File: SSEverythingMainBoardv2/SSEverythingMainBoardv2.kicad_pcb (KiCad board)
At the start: 4 copper layers, 99.1 x 81.3 mm, 71 parts, among them J1 CONN_06SILK_FEMALE_PTH, J2 CONN_06SILK_FEMALE_PTH, J4 Switch, J5 Conn_01x02, J6 Conn_01x05, J8 Conn_01x03, M1 Left MOTOR, M2 Right MOTOR, Q1 PBSS4160DS, Q2 PBSS4160DS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

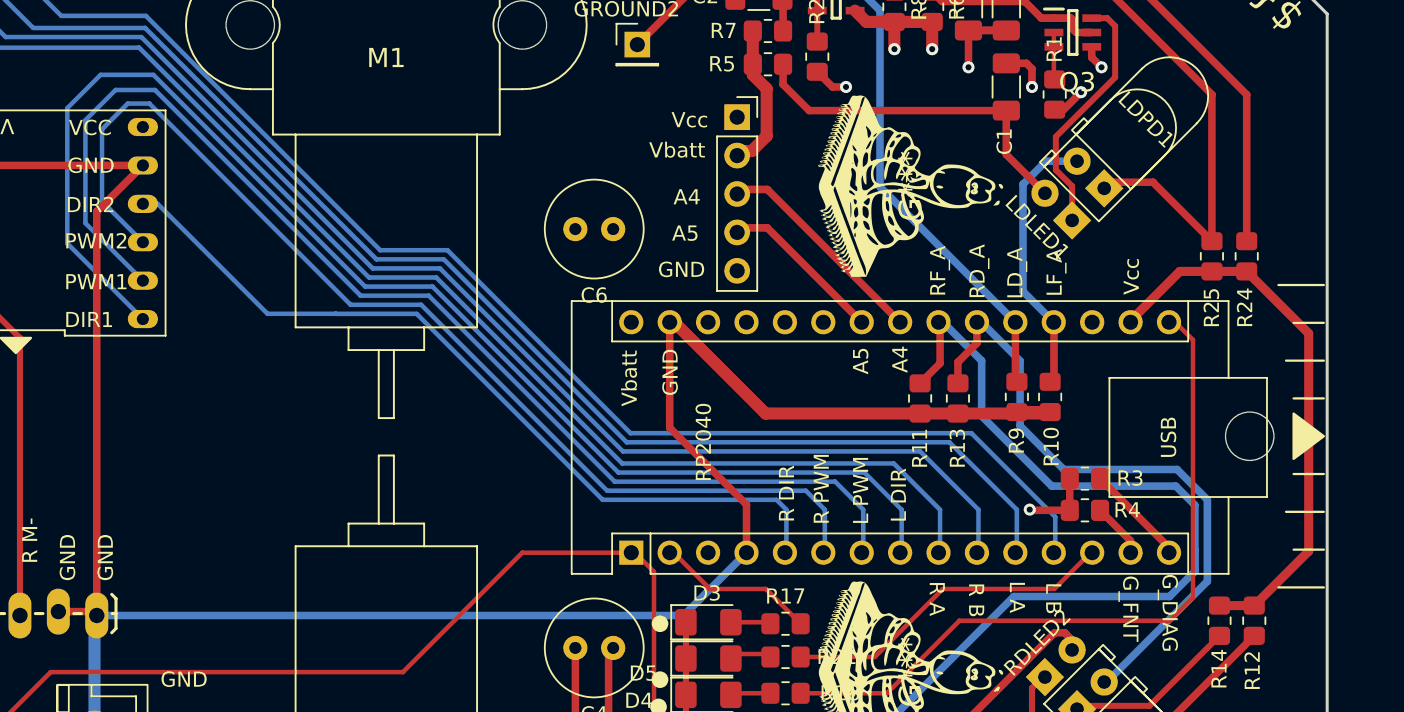
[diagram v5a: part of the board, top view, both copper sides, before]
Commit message: trace tweaks
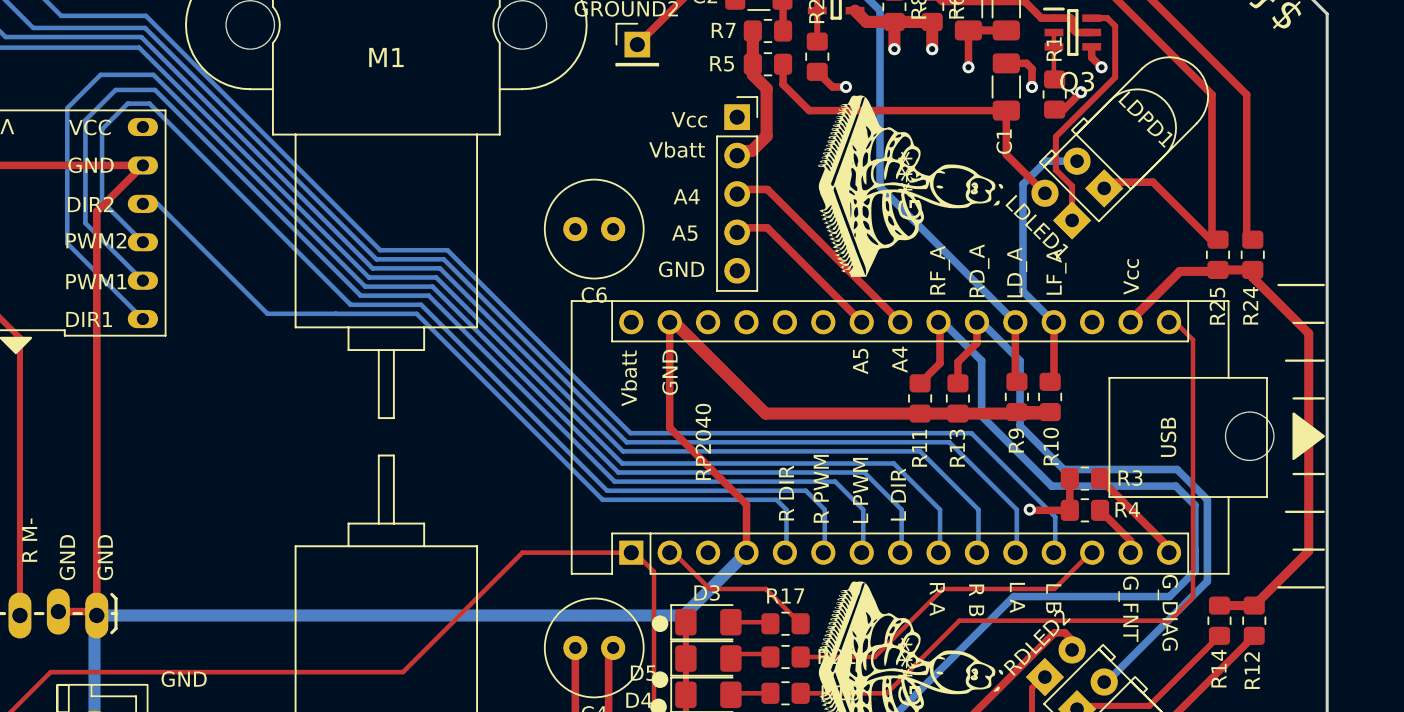
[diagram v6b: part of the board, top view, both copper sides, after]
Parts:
- moved R24 0.41 mm to (162.3, 93.0)
- moved R25 0.41 mm to (160.0, 93.0)
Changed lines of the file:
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@@
 	(footprint "Resistor_SMD:R_0805_2012Metric_Pad1.20x1.40mm_HandSolder"
 		(layer "F.Cu")
-		(at 161.9 93.1 -90)
+		(at 162.3 93 -90)
 		(descr "Resistor SMD 0805 (2012 Metric), square (rectangular) end terminal, IPC-7351 nominal with elongated pad for handsoldering. (Body size source: IPC-SM-782 page 72, https://www.pcb-3d.com/wordpress/wp-content/uploads/ipc-sm-782a_amendment_1_and_2.pdf), generated with kicad-footprint-generator")
 		(tags "resistor handsolder")
@@
 		(fp_poly
 			(pts
-				(xy -1.94 -1.21) (xy 4.49 -1.21) (xy 4.49 10.18) (xy -1.94 10.179997)
+				(xy -1.94 -1.21) (xy 4.49 -1.21) (xy 4.49 10.18) (xy -1.94 10.179999)
 			)
 			(stroke
@@
 		(fp_poly
 			(pts
-				(xy -1.94 -1.21) (xy 4.49 -1.21) (xy 4.49 10.18) (xy -1.94 10.179997)
+				(xy -1.94 -1.21) (xy 4.49 -1.21) (xy 4.49 10.18) (xy -1.94 10.179999)
 			)
 			(stroke
@@
 		(fp_poly
 			(pts
-				(xy -1.94 -1.21) (xy 4.490002 -1.21) (xy 4.49 10.18) (xy -1.94 10.18)
+				(xy -1.94 -1.21) (xy 4.490001 -1.21) (xy 4.49 10.18) (xy -1.94 10.18)
 			)
 			(stroke
@@
 		(fp_line
 			(start -1.23 1.27)
-			(end -1.229998 7.37)
+			(end -1.229999 7.37)
 			(stroke
 				(width 0.1)
@@
 			(start 3.77 7.37)
 			(mid 1.27 9.87)
-			(end -1.229998 7.37)
+			(end -1.229999 7.37)
 			(stroke
 				(width 0.1)
@@
 	(footprint "Resistor_SMD:R_0805_2012Metric_Pad1.20x1.40mm_HandSolder"
 		(layer "F.Cu")
-		(at 159.6 93.1 -90)
+		(at 160 93 -90)
 		(descr "Resistor SMD 0805 (2012 Metric), square (rectangular) end terminal, IPC-7351 nominal with elongated pad for handsoldering. (Body size source: IPC-SM-782 page 72, https://www.pcb-3d.com/wordpress/wp-content/uploads/ipc-sm-782a_amendment_1_and_2.pdf), generated with kicad-footprint-generator")
 		(tags "resistor handsolder")
@@
 		(fp_poly
 			(pts
-				(xy -1.94 -1.21) (xy 4.490002 -1.21) (xy 4.49 10.18) (xy -1.94 10.18)
+				(xy -1.94 -1.21) (xy 4.490001 -1.21) (xy 4.49 10.18) (xy -1.94 10.18)
 			)
 			(stroke
@@
 		(fp_line
 			(start -1.23 1.27)
-			(end -1.229998 7.37)
+			(end -1.229999 7.37)
 			(stroke
 				(width 0.1)
@@
 			(start 3.77 7.37)
 			(mid 1.27 9.87)
-			(end -1.229998 7.37)
+			(end -1.229999 7.37)
 			(stroke
 				(width 0.1)
@@
 		(start 85.85 116.854)
 		(end 124.666 116.854)
-		(width 0.5)
+		(width 0.8)
 		(layer "B.Cu")
 		(net 1)
@@
 		(start 124.666 116.854)
 		(end 128.82 112.7)
-		(width 0.5)
+		(width 0.8)
 		(layer "B.Cu")
 		(net 1)
@@
 	)
 	(segment
-		(start 88.5 103.6)
-		(end 86.644946 101.744946)
-		(width 0.8)
-		(layer "In1.Cu")
-		(net 2)
-	)
-	(segment
-		(start 86.905789 136.359211)
-		(end 82.465 140.8)
-		(width 0.8)
-		(layer "In1.Cu")
-		(net 2)
-	)
-	(segment
-		(start 88.5 120.1)
-		(end 88.5 103.6)
-		(width 0.8)
-		(layer "In1.Cu")
-		(net 2)
-	)
-	(segment
-		(start 86.611108 96.311108)
-		(end 74.85 84.55)
+		(start 97.3 123.2)
+		(end 91.999 128.501)
 		(width 0.8)
 		(layer "In1.Cu")
@@
 	)
 	(segment
-		(start 87.376 135.889)
-		(end 87.376 121.224)
+		(start 88.5 134.765)
+		(end 88.5 101)
 		(width 0.8)
 		(layer "In1.Cu")
@@
 	)
 	(segment
+		(start 120 119)
+		(end 115.8 123.2)
+		(width 0.8)
+		(layer "In1.Cu")
+		(net 2)
+	)
+	(segment
 		(start 121.2 97.46)
 		(end 121.3 97.56)
@@
 	)
 	(segment
-		(start 120 119)
-		(end 102.640789 136.359211)
+		(start 82.465 140.8)
+		(end 88.5 134.765)
 		(width 0.8)
 		(layer "In1.Cu")
@@
 	)
 	(segment
-		(start 87.376 121.224)
-		(end 88.5 120.1)
+		(start 72.05 84.55)
+		(end 71.9 84.55)
 		(width 0.8)
 		(layer "In1.Cu")
@@
 	)
 	(segment
-		(start 86.611108 101.778784)
-		(end 86.611108 96.311108)
+		(start 88.5 101)
+		(end 72.05 84.55)
 		(width 0.8)
 		(layer "In1.Cu")
@@
 	)
 	(segment
-		(start 119.2 118.477541)
-		(end 119.732771 119.010312)
-		(width 1)
+		(start 91.999 128.501)
+		(end 91.999 131.266)
+		(width 0.8)
 		(layer "In1.Cu")
 		(net 2)
 	)
 	(segment
-		(start 86.644946 101.744946)
-		(end 86.611108 101.778784)
-		(width 0.8)
+		(start 119.2 118.477541)
+		(end 119.732771 119.010312)
+		(width 1)
 		(layer "In1.Cu")
 		(net 2)
@@
 	)
 	(segment
-		(start 82.465 140.8)
-		(end 87.376 135.889)
-		(width 0.8)
-		(layer "In1.Cu")
-		(net 2)
-	)
-	(segment
-		(start 74.85 84.55)
-		(end 71.9 84.55)
+		(start 91.999 131.266)
+		(end 82.465 140.8)
 		(width 0.8)
 		(layer "In1.Cu")
@@
 	)
 	(segment
-		(start 102.640789 136.359211)
-		(end 86.905789 136.359211)
+		(start 115.8 123.2)
+		(end 97.3 123.2)
 		(width 0.8)
 		(layer "In1.Cu")
@@
 	)
 	(segment
-		(start 154.22 97.46)
-		(end 154.32 97.36)
+		(start 154.32 97.26)
+		(end 157.48 94.1)
 		(width 0.6)
 		(layer "F.Cu")
@@
 	)
 	(segment
-		(start 166.001 112.599)
-		(end 162.4 116.2)
+		(start 154.22 97.46)
+		(end 154.32 97.36)
+		(width 0.6)
+		(layer "F.Cu")
+		(net 4)
+	)
+	(segment
+		(start 166.001 98.201)
+		(end 166.001 112.599)
+		(width 0.6)
+		(layer "F.Cu")
+		(net 4)
+	)
+	(segment
+		(start 157.48 94.1)
+		(end 159.9 94.1)
 		(width 0.6)
 		(layer "F.Cu")
@@
 	)
 	(segment
-		(start 161.9 94.1)
-		(end 166.001 98.201)
+		(start 162.3 94)
+		(end 162.3 94.5)
 		(width 0.6)
 		(layer "F.Cu")
@@
 	)
 	(segment
-		(start 154.32 97.26)
-		(end 157.48 94.1)
+		(start 160 94)
+		(end 162.3 94)
 		(width 0.6)
 		(layer "F.Cu")
@@
 	)
 	(segment
-		(start 157.48 94.1)
-		(end 159.6 94.1)
+		(start 162.3 94.5)
+		(end 166.001 98.201)
 		(width 0.6)
 		(layer "F.Cu")
@@
 	)
 	(segment
-		(start 166.001 98.201)
-		(end 166.001 112.599)
+		(start 166.001 112.599)
+		(end 162.4 116.2)
 		(width 0.6)
 		(layer "F.Cu")
@@
 	)
 	(segment
-		(start 159.6 94.1)
-		(end 161.9 94.1)
+		(start 159.9 94.1)
+		(end 160 94)
 		(width 0.6)
 		(layer "F.Cu")
@@
 	)
 	(segment
-		(start 146 75.0375)
-		(end 146.3885 74.649)
+		(start 159.6 82.4)
+		(end 159.6 91.6)
 		(width 0.5)
 		(layer "F.Cu")
@@
 	)
 	(segment
-		(start 159.6 92.1)
-		(end 155.7 88.2)
+		(start 155.7 88.2)
+		(end 152.881683 88.2)
 		(width 0.5)
 		(layer "F.Cu")
@@
 	)
 	(segment
-		(start 155.7 88.2)
-		(end 152.881683 88.2)
+		(start 159.5 92)
+		(end 155.7 88.2)
 		(width 0.5)
 		(layer "F.Cu")
@@
 	)
 	(segment
-		(start 152.881683 88.2)
-		(end 152.475163 88.60652)
+		(start 159.6 91.6)
+		(end 160 92)
 		(width 0.5)
 		(layer "F.Cu")
@@
 	)
 	(segment
-		(start 159.6 82.4)
-		(end 159.6 92.1)
+		(start 160 92)
+		(end 159.5 92)
+		(width 0.5)
+		(layer "F.Cu")
+		(net 26)
+	)
+	(segment
+		(start 146 75.0375)
+		(end 146.3885 74.649)
 		(width 0.5)
 		(layer "F.Cu")
@@
 	)
 	(segment
+		(start 152.881683 88.2)
+		(end 152.475163 88.60652)
+		(width 0.5)
+		(layer "F.Cu")
+		(net 26)
+	)
+	(segment
 		(start 134.44258 73.39258)
 		(end 136 74.95)
@@
 	)
 	(segment
+		(start 129.26778 71.8)
+		(end 141.5 71.8)
+		(width 0.5)
+		(layer "F.Cu")
+		(net 44)
+	)
+	(segment
 		(start 153.314572 73.824)
 		(end 144.7135 73.824)
@@
 	)
 	(segment
-		(start 129.26778 71.8)
-		(end 141.5 71.8)
+		(start 161.9 91.6)
+		(end 161.9 82.409428)
 		(width 0.5)
 		(layer "F.Cu")
@@
 	)
 	(segment
-		(start 144.7135 73.824)
+		(start 143.5 73.8)
 		(end 143.5 75.0375)
 		(width 0.5)
@@
 	)
 	(segment
-		(start 161.9 92.1)
-		(end 161.9 82.409428)
+		(start 161.9 82.409428)
+		(end 153.314572 73.824)
 		(width 0.5)
 		(layer "F.Cu")
@@
 	)
 	(segment
-		(start 143.5 73.8)
-		(end 143.5 75.0375)
+		(start 141.5 71.8)
+		(end 143.5 73.8)
 		(width 0.5)
 		(layer "F.Cu")
@@
 	)
 	(segment
-		(start 141.5 71.8)
-		(end 143.5 73.8)
+		(start 162.3 92)
+		(end 161.9 91.6)
 		(width 0.5)
 		(layer "F.Cu")
@@
 	)
 	(segment
-		(start 161.9 82.409428)
-		(end 153.314572 73.824)
+		(start 144.7135 73.824)
+		(end 143.5 75.0375)
 		(width 0.5)
 		(layer "F.Cu")
@@
 	)
 	(group ""
-		(members "0981775e-9594-4afc-b9cb-a2d4fe6db366" "3bd5a070-f3d6-4033-8048-246fa37a1c7b"
-			"5ccf1642-07db-4e6b-af92-64bb91fb7052" "64139186-3749-40d5-a96a-ddb0e4cf9d8e"
+		(members "41a56526-267b-4358-9221-53ff4bff03e4" "5ccf1642-07db-4e6b-af92-64bb91fb7052"
+			"64139186-3749-40d5-a96a-ddb0e4cf9d8e" "6bb6b209-97c7-4206-8446-92417e5064fb"
 		)
 	)

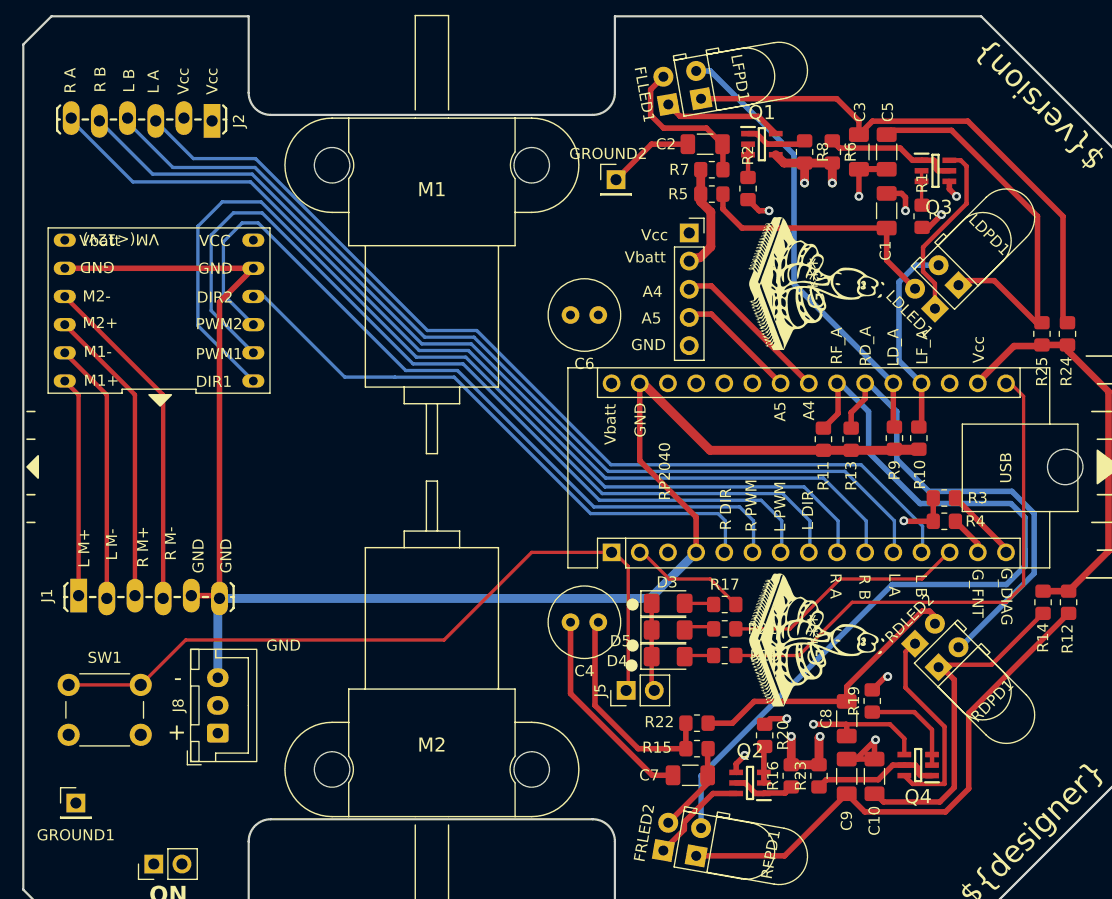
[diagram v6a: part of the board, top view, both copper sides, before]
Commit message: New board sent to JLCPCB for new Chassis
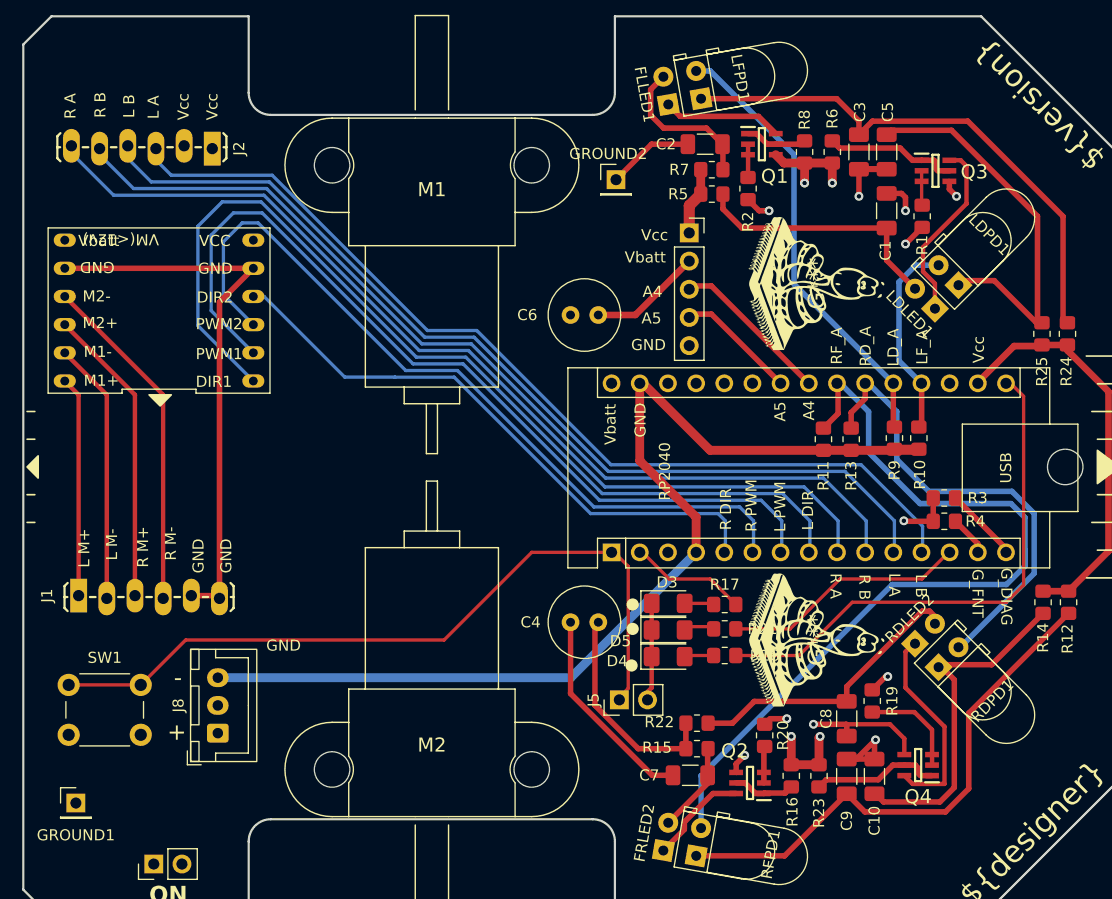
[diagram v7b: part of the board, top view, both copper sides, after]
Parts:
- moved J2 2.50 mm to (85.2, 76.3)
- moved J5 1.05 mm to (121.9, 126.0)
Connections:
- J6 pad 1: Vcc -> Vbatt
- J6 pad 2: Vbatt -> Vcc
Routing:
- net Vcc: track 128.8 -> 124.3 mm
- net GND: track 243.6 -> 240.6 mm
- net Net-(A1-D1/TX): track 67.2 -> 68.3 mm
- net RIGHT_ENC_A: track 87.2 -> 86.4 mm
- net RIGHT_ENC_B: track 87.0 -> 86.2 mm
- net LEFT_ENC_A: track 87.3 -> 86.7 mm
